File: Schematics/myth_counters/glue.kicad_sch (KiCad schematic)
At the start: 7 parts, among them U1 74LS08, U22 74LS08, U3 4072, U4 74HC74, U5 74HC02, U6 74HC00, U7 74LS32

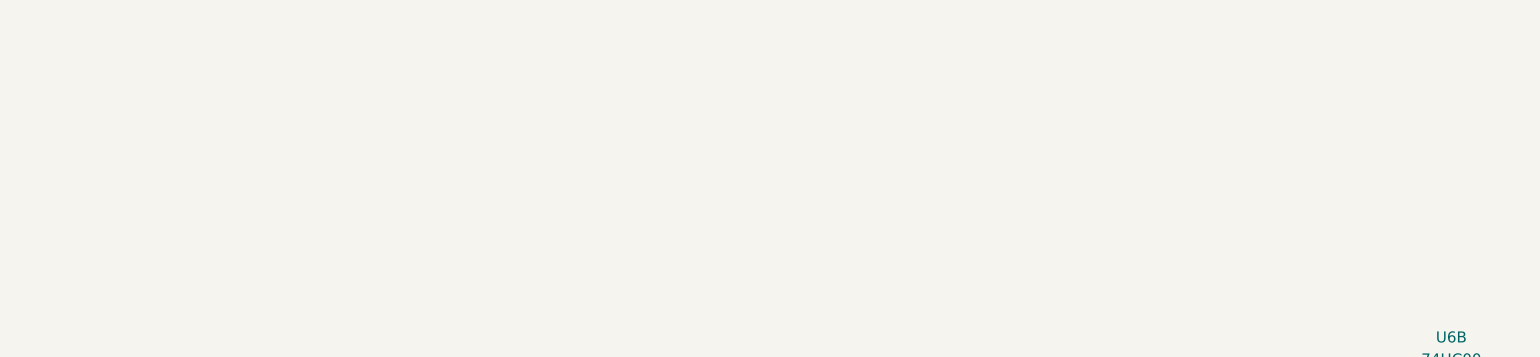
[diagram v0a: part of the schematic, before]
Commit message: Change d to g
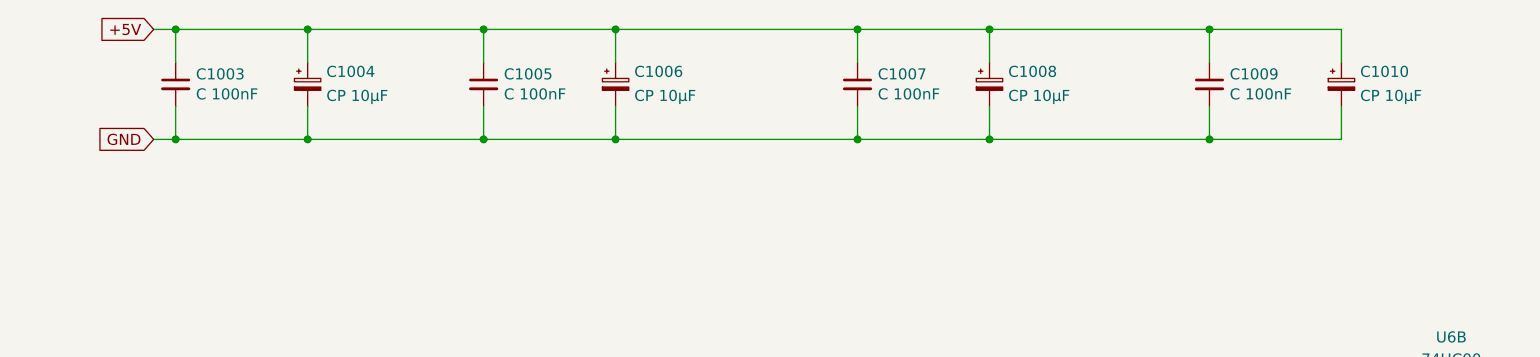
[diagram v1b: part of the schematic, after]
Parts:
- added C1003, C1005, C1007, C1009: C 100nF, Capacitor_THT:C_Disc_D5.0mm_W2.5mm_P2.50mm, symbol Device:C_Small
- added C1004, C1006, C1008, C1010: CP 10μF, Capacitor_THT:CP_Radial_D6.3mm_P2.50mm, symbol Device:C_Polarized_Small
- U1, U22, U3, U4, U5, U6, U7: footprint (none) -> Package_DIP:DIP-14_W7.62mm_LongPads
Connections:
- net +5V: now also C1003.1, C1004.1, C1005.1, C1006.1, C1007.1, C1008.1, C1009.1, C1010.1
- net GND: now also C1003.2, C1004.2, C1005.2, C1006.2, C1007.2, C1008.2, C1009.2, C1010.2

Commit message: Change signal names
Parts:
- added U1001: 74LS08, Package_DIP:DIP-14_W7.62mm_LongPads, symbol 74xx:74LS08
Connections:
- net GND: now also U1001.12, U1001.13
- no-connect marks 11 -> 12
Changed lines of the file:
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@@
+	)
+	(no_connect
+		(at 134.62 64.77)
 	)
 	(no_connect
@@
 				)
 				(justify left)
+				(hide yes)
+			)
+		)
+	)
+	(global_label "GND"
+		(shape input)
+		(at 119.38 67.31 180)
+		(fields_autoplaced yes)
+		(effects
+			(font
+				(size 1.27 1.27)
+			)
+			(justify right)
+		)
+		(property "Intersheetrefs" "${INTERSHEET_REFS}"
+			(at 112.5243 67.31 0)
+			(effects
+				(font
+					(size 1.27 1.27)
+				)
+				(justify right)
+				(hide yes)
+			)
+		)
+	)
+	(global_label "GND"
+		(shape input)
+		(at 119.38 62.23 180)
+		(fields_autoplaced yes)
+		(effects
+			(font
+				(size 1.27 1.27)
+			)
+			(justify right)
+		)
+		(property "Intersheetrefs" "${INTERSHEET_REFS}"
+			(at 112.5243 62.23 0)
+			(effects
+				(font
+					(size 1.27 1.27)
+				)
+				(justify right)
 				(hide yes)
 			)
@@
 				)
 			)
+		)
+	)
+	(symbol
+		(lib_id "74xx:74LS08")
+		(at 127 64.77 0)
+		(unit 4)
+		(exclude_from_sim no)
+		(in_bom yes)
+		(on_board yes)
+		(dnp no)
+		(fields_autoplaced yes)
+		(property "Reference" "U1001"
+			(at 126.9917 55.88 0)
+			(effects
+				(font
+					(size 1.27 1.27)
+				)
+			)
+		)
+		(property "Value" "74LS08"
+			(at 126.9917 58.42 0)
+			(effects
+				(font
+					(size 1.27 1.27)
+				)
+			)
+		)
+		(property "Footprint" "Package_DIP:DIP-14_W7.62mm_LongPads"
+			(at 127 64.77 0)
+			(effects
+				(font
+					(size 1.27 1.27)
+				)
+				(hide yes)
+			)
+		)
+		(property "Datasheet" "http://www.ti.com/lit/gpn/sn74LS08"
+			(at 127 64.77 0)
+			(effects
+				(font
+					(size 1.27 1.27)
+				)
+				(hide yes)
+			)
+		)
+		(property "Description" "Quad And2"
+			(at 127 64.77 0)
+			(effects
+				(font
+					(size 1.27 1.27)
+				)
+				(hide yes)
+			)
+		)
+		(pin "8"
+		)
+		(pin "2"
+		)
+		(pin "9"
+		)
+		(pin "11"
+		)
+		(pin "12"
+		)
+		(pin "13"
+		)
+		(pin "14"
+		)
+		(pin "7"
+		)
+		(pin "3"
+		)
+		(pin "1"
+		)
+		(pin "5"
+		)
+		(pin "4"
+		)
+		(pin "10"
+		)
+		(pin "6"
+		)
+		(instances
+			(project "myth_counters"
+				(path "/c50a2a1f-7d02-4e47-8cba-362a907cb5f7/952f1025-bd15-4fc8-84e2-a82136def1dc"
+					(reference "U1001")
+					(unit 4)
+				)
+			)
